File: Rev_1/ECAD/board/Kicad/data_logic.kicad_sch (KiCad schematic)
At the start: 75 parts, among them SW300 6x6, SW301 6x6, SW302 6x6, SW303 6x6, U301 74HC245, U303 74HC245, U304 74HC595, U305 74HC595, U306 74HC595, U307 AT28C64B-15PU, U308 Summer

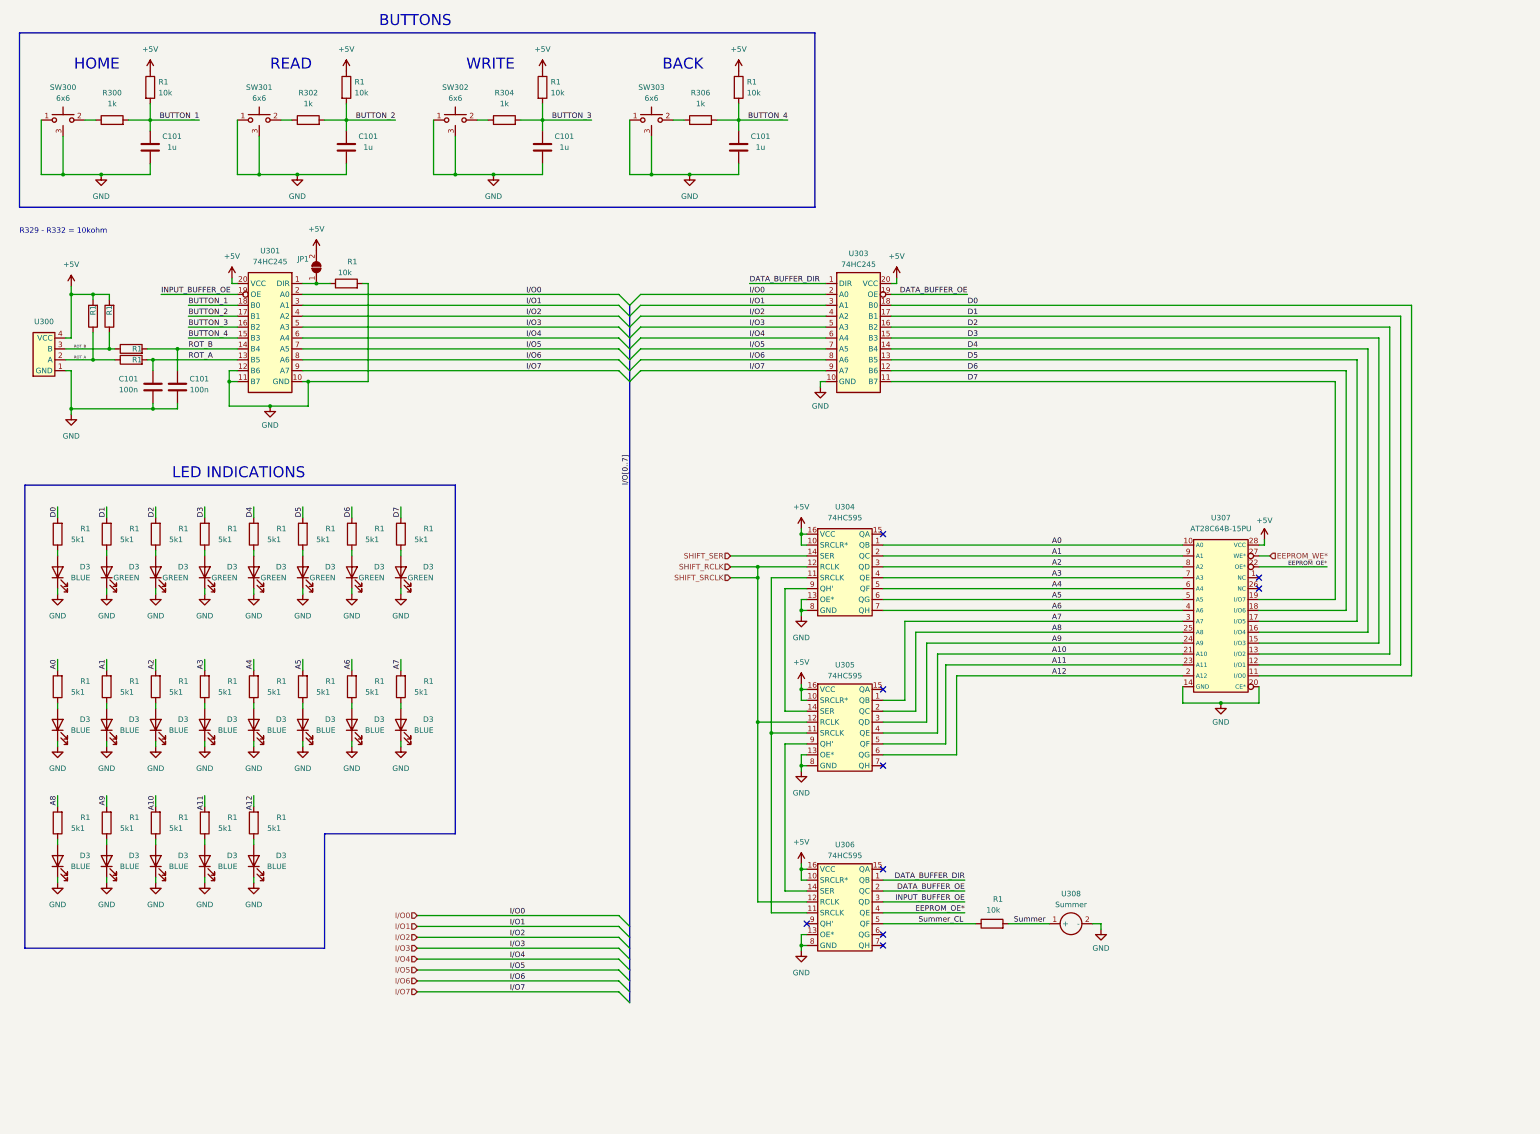
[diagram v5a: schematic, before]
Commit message: Added Bypass Capacitors
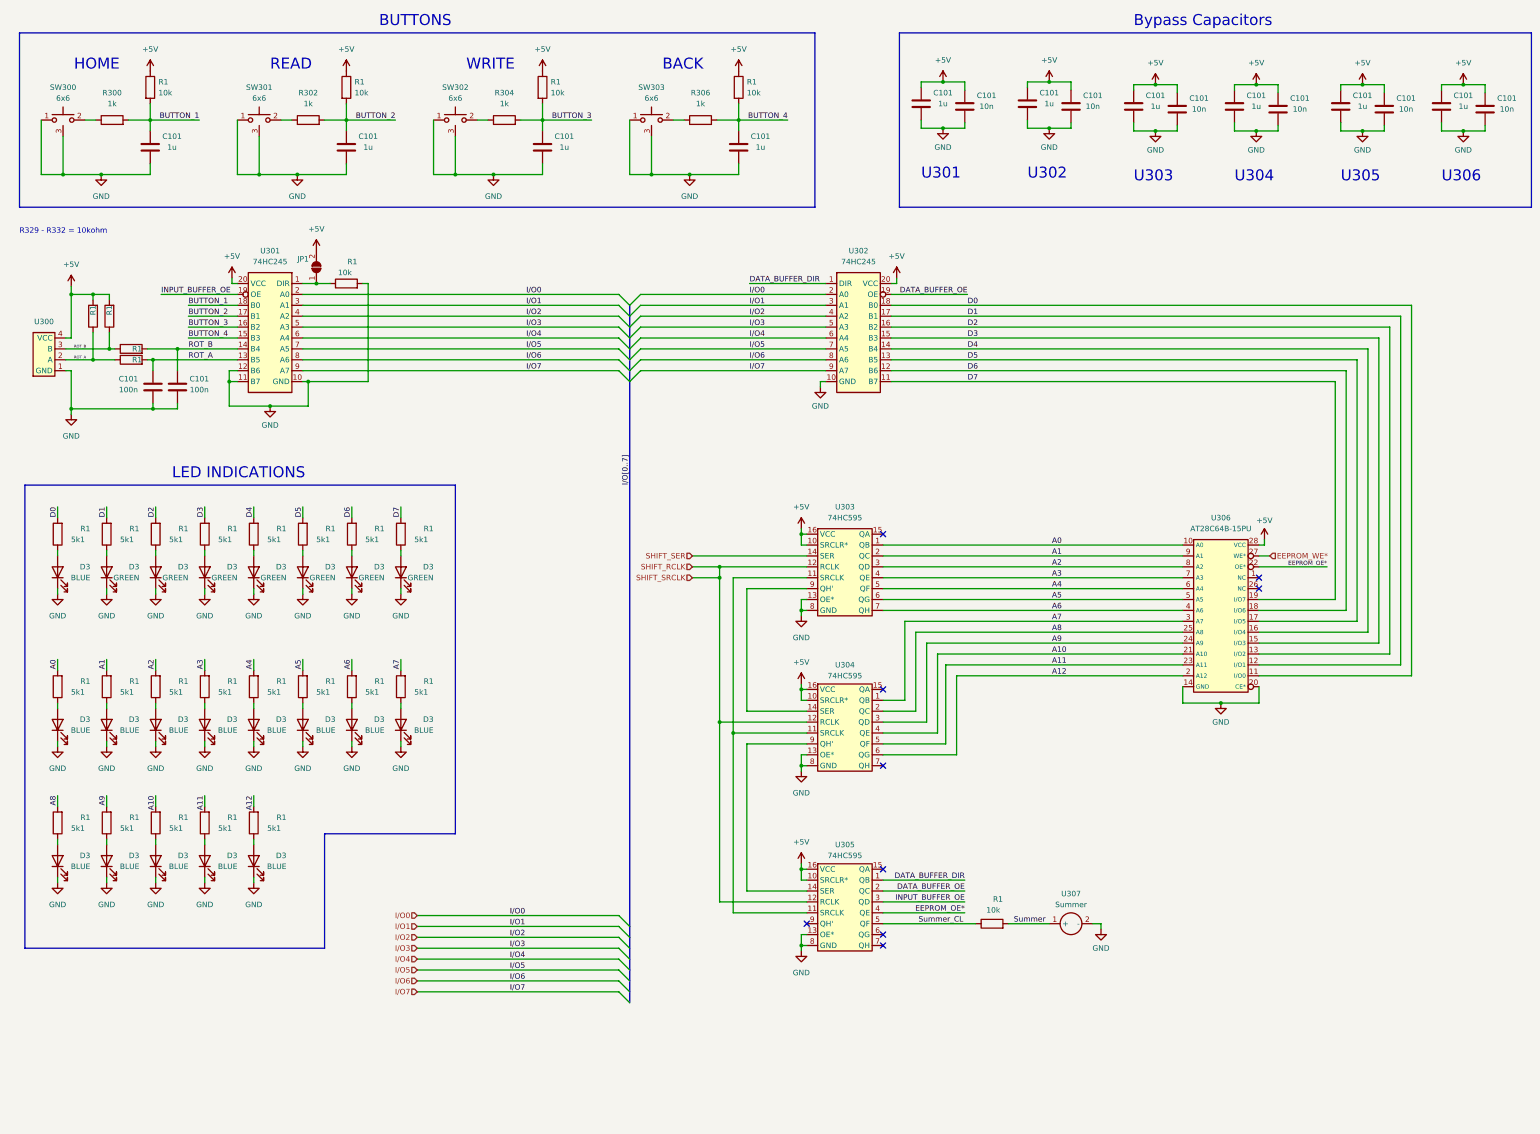
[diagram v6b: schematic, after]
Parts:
- added C101 (x6): 10n, Capacitor_SMD:C_0805_2012Metric_Pad1.18x1.45mm_HandSolder, symbol Device:C
- added C101 (x6): 1u, Capacitor_SMD:C_0805_2012Metric_Pad1.18x1.45mm_HandSolder, symbol Device:C
- renumbered U303 to U302, U304 to U303, U305 to U304, U306 to U305, U307 to U306, U308 to U307
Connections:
- net +5V: now also C101.2, C101.2, C101.2, C101.2, C101.2, C101.2, C101.2, C101.2, C101.2, C101.2, C101.2, C101.2
- net GND: now also C101.1, C101.1, C101.1, C101.1, C101.1, C101.1, C101.1, C101.1, C101.1, C101.1, C101.1, C101.1
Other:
- note added: "Bypass Capacitors"
- note added: "U301"
- note added: "U302"
- note added: "U303"
- note added: "U304"
- note added: "U305"
- note added: "U306"
